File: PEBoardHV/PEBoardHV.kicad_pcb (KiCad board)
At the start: 2 copper layers, 40 parts, among them J1 To PE LV, J2 Left Connector (Master), J3 E-Meter Internal, J4 Right Connector (Slave), J5 E-Meter External, J6 HV Cable, J7 TSMPs, J8 HV CAN Debug, J9 EMeter HV, U1 L78S05CV-DG, U2 ISO1050, U3 PS2501-4, U4 DK1A1B-12V, U5 DK1A1B-12V

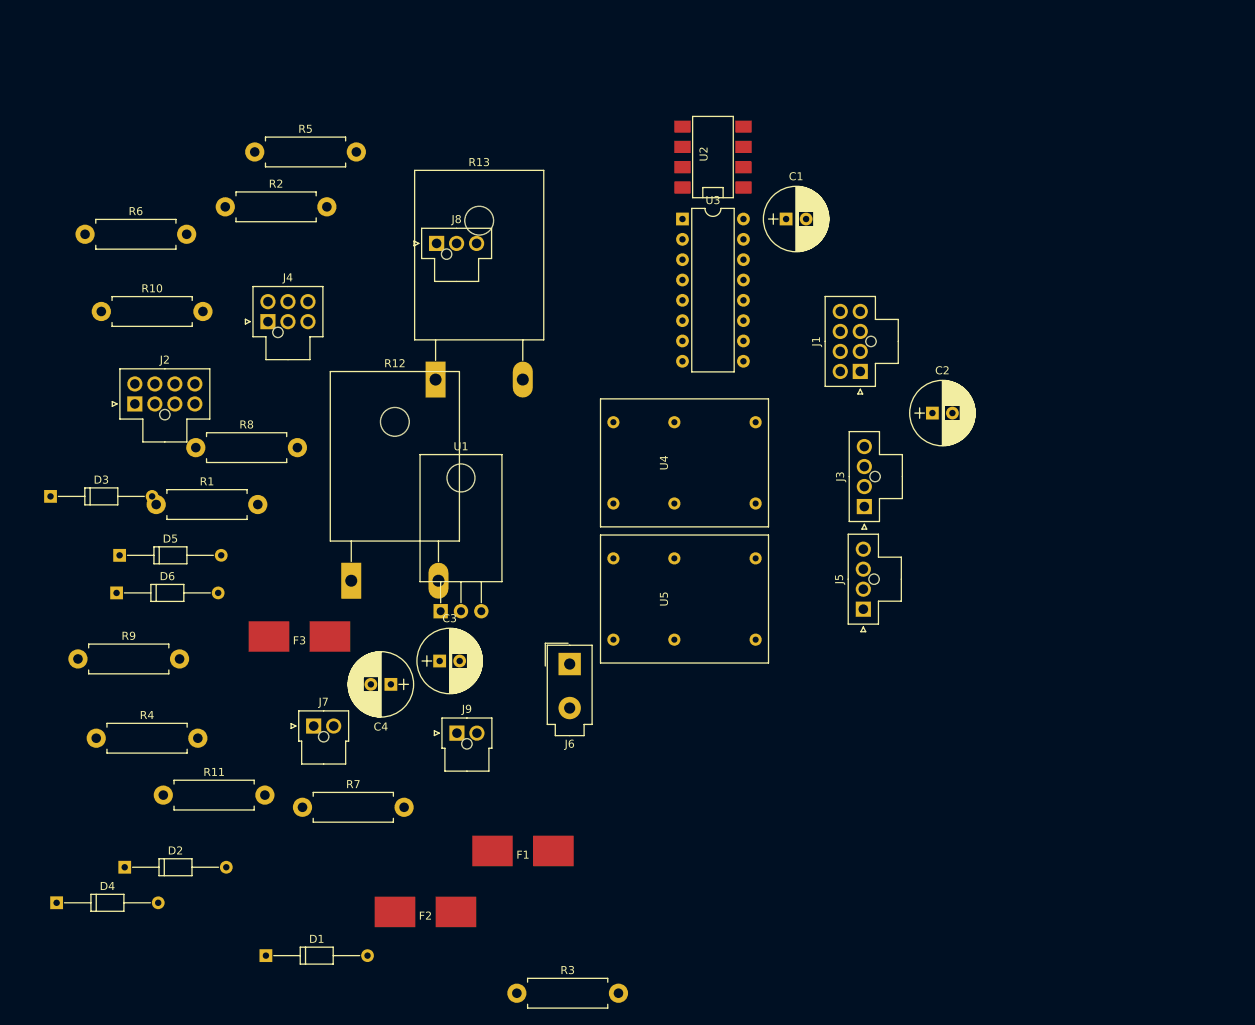
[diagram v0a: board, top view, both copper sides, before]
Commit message: Progress on PE HV PCB layout
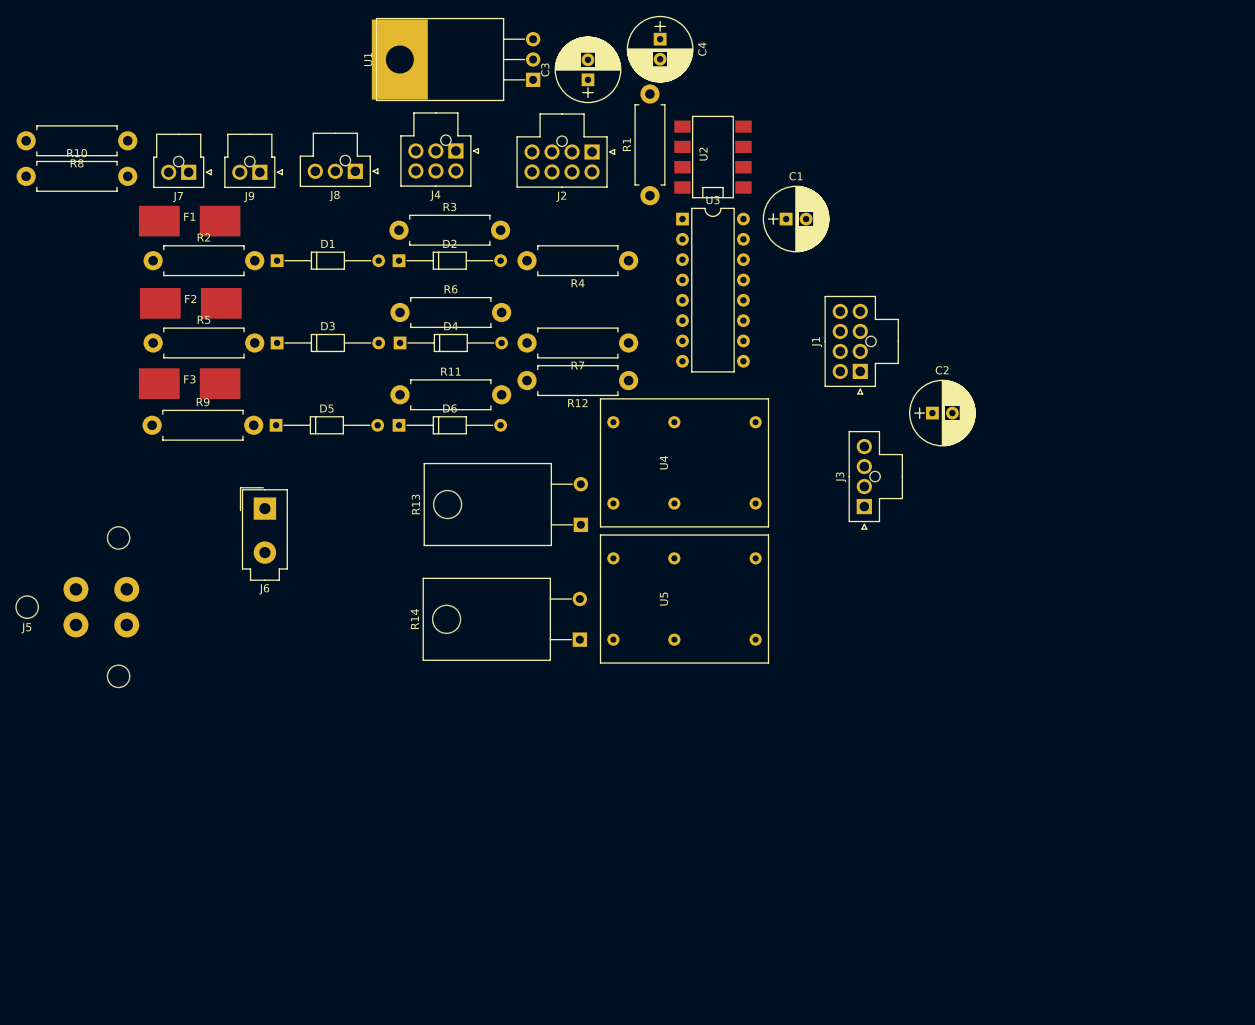
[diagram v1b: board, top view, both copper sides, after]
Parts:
- added R14: 1K, TO_SOT_Packages_THT:TO-220-2_Horizontal, F.Cu at (145.9, 112.8)
- J5: footprint Connectors_Molex:Molex_NanoFit_1x04x2.50mm_Straight -> FSFootprints:DT13-4P
- R1: value R -> 120
- R10: value 1.2kR -> 5kR
- R11, R3, R6: value 3kR -> 1.2kR
- R12: value 1K -> 3kR; footprint TO_SOT_Packages_THT:TO-247-2_Horizontal -> Resistors_THT:R_Axial_DIN0411_L9.9mm_D3.6mm_P12.70mm_Horizontal
- R13: footprint TO_SOT_Packages_THT:TO-247-2_Horizontal -> TO_SOT_Packages_THT:TO-220-2_Horizontal
- R2, R5: value 1.2kR -> R
- R4: value R -> 3kR
- R7: value 5kR -> 3kR
- R8: value R -> 5kR
- R9: value 5kR -> R
- U1: footprint TO_SOT_Packages_THT:TO-220-3_Horizontal -> FSFootprints:TO-220-3_Horizontal_HeatSunk
- moved J5 104.5 mm to (76.8, 108.7), turned to 0 degrees
- moved R3 96.5 mm to (123.3, 61.6)
- moved R4 89.4 mm to (152.0, 65.4), turned to 180 degrees
- moved F1 89.1 mm to (97.2, 60.5), turned to 180 degrees
- moved C4 87.4 mm to (156.0, 37.7), turned to 270 degrees
- moved D1 86.9 mm to (108.1, 65.4)
- moved D2 83.2 mm to (123.3, 65.4)
- moved D4 82.1 mm to (123.4, 75.7)
- moved F2 81.5 mm to (97.3, 70.7), turned to 180 degrees
- moved C3 75.0 mm to (146.9, 42.8), turned to 90 degrees
- moved J9 74.3 mm to (105.9, 54.4), turned to 180 degrees
- moved R1 72.8 mm to (154.7, 57.3), turned to 90 degrees
- moved J7 71.0 mm to (97.0, 54.4), turned to 180 degrees
- moved R7 70.9 mm to (152.0, 75.7), turned to 180 degrees
- moved U1 67.4 mm to (140.1, 42.8), turned to 90 degrees
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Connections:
- J2 pad 8: Net-(J2-Pad8) -> (no net)
- R1 pad 1: Net-(F1-Pad2) -> /CAN_H_BOARD
- R1 pad 2: Net-(D1-Pad1) -> /CAN_L_BOARD
- R10 pad 1: Net-(D5-Pad2) -> /TS-
- R10 pad 2: Net-(R10-Pad2) -> Net-(J7-Pad2)
- R11 pad 1: /TS- -> Net-(D5-Pad2)
- R11 pad 2: Net-(D6-Pad2) -> Net-(R11-Pad2)
- R12 pad 1: /TS+_SWITCHED_L -> /TS-
- R12 pad 2: Net-(R12-Pad2) -> Net-(D6-Pad2)
- R13 pad 1: /TS+_SWITCHED_R -> /TS-
- R2 pad 1: Net-(D1-Pad2) -> Net-(F1-Pad2)
- R2 pad 2: Net-(R2-Pad2) -> Net-(D1-Pad1)
- R3 pad 1: /TS- -> Net-(D1-Pad2)
- R3 pad 2: Net-(D2-Pad2) -> Net-(R3-Pad2)
- R4 pad 1: Net-(F2-Pad2) -> /TS-
- R4 pad 2: Net-(D3-Pad1) -> Net-(D2-Pad2)
- R5 pad 1: Net-(D3-Pad2) -> Net-(F2-Pad2)
- R5 pad 2: Net-(R5-Pad2) -> Net-(D3-Pad1)
- R6 pad 1: /TS- -> Net-(D3-Pad2)
- R6 pad 2: Net-(D4-Pad2) -> Net-(R6-Pad2)
- R7 pad 1: Net-(J7-Pad1) -> /TS-
- R7 pad 2: /TS+_FUSED -> Net-(D4-Pad2)
- R8 pad 1: /TS+_FUSED -> Net-(J7-Pad1)
- R8 pad 2: Net-(D5-Pad1) -> /TS+_FUSED
- R9 pad 1: /TS- -> /TS+_FUSED
- R9 pad 2: Net-(J7-Pad2) -> Net-(D5-Pad1)
- U2 pad 1: /3.3V_LV -> (no net)
- U3 pad 1: Net-(R2-Pad2) -> Net-(R3-Pad2)
- U3 pad 3: Net-(R5-Pad2) -> Net-(R6-Pad2)
- U3 pad 5: Net-(R10-Pad2) -> Net-(R11-Pad2)
- U4 pad 3: Net-(U4-Pad3) -> (no net)
- U4 pad 4: Net-(U4-Pad4) -> (no net)
- U4 pad 5: Net-(R12-Pad2) -> /TS+_SWITCHED_L
- U4 pad 6: /TS- -> Net-(R13-Pad2)
- U5 pad 3: Net-(U5-Pad3) -> (no net)
- U5 pad 4: Net-(U5-Pad4) -> (no net)
- U5 pad 5: Net-(R13-Pad2) -> /TS+_SWITCHED_R
- U5 pad 6: /TS- -> Net-(R14-Pad2)

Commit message: Layout and route PE HV board
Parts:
- added C5: CP, Capacitors_THT:CP_Radial_D8.0mm_P2.50mm, F.Cu at (110.7, 89.7)
- C1: value C -> CP
- C3: value CP -> C
- J6: footprint Connectors_Molex:Molex_MiniFit-JR-5556-02A_2x01x4.20mm_Straight -> Connectors_Molex:Molex_NanoFit_1x02x2.50mm_Straight
- J7: footprint Connectors_Molex:Molex_NanoFit_1x02x2.50mm_Straight -> FSFootprints:DT15-2P; moved to B.Cu
- R13, R14: footprint TO_SOT_Packages_THT:TO-220-2_Horizontal -> TO_SOT_Packages_THT:TO-220-2_Vertical
- moved R10 73.2 mm to (120.9, 113.2)
- moved C4 67.6 mm to (124.2, 97.4)
- moved U1 58.2 mm to (115.4, 95.5), turned to 180 degrees
- moved J7 45.2 mm to (125.9, 89.2), turned to 0 degrees
- moved J6 42.5 mm to (98.6, 54.6), turned to 180 degrees
- moved R8 35.9 mm to (119.3, 70.4)
- moved C3 29.8 mm to (173.5, 56.4)
- moved R9 27.8 mm to (88.1, 58.5), turned to 270 degrees
- moved R5 26.0 mm to (118.2, 79.6), turned to 180 degrees
- moved C1 24.2 mm to (147.7, 57.5), turned to 90 degrees
- moved F3 21.8 mm to (82.4, 64.8), turned to 90 degrees
- moved C2 16.3 mm to (175.3, 77.6), turned to 180 degrees
- moved R14 11.7 mm to (144.8, 101.1), turned to 180 degrees
- moved J1 10.9 mm to (175.0, 70.1)
- moved J3 7.69 mm to (174.4, 93.2)
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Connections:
- C1 pad 1: /5V_GLV -> /5V_TS
- C1 pad 2: GND -> /TS-
- C2 pad 1: /3.3V_GLV -> /5V_GLV
- C3 pad 1: /CAN+ -> /3.3V_GLV
- C3 pad 2: /TS- -> GND
- C4 pad 1: /5V_TS -> /CAN+
- U2 pad 1: (no net) -> /3.3V_GLV
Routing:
- net GND: track 0.00 -> 186.6 mm
- net /TS-: track 0.00 -> 181.7 mm, vias 0 -> 1
- net +12V: track 0.00 -> 146.4 mm
- net /EM_SIG-: track 0.00 -> 126.3 mm
- net /EM_SIG+: track 0.00 -> 122.2 mm
- net /TS+_SWITCHED_R: track 0.00 -> 97.8 mm
- net /TS+_SWITCHED_L: track 0.00 -> 92.5 mm
- net /5V_TS: track 0.00 -> 84.4 mm
- net /TS+: track 0.00 -> 71.2 mm, vias 0 -> 1
- net /CAN+: track 0.00 -> 64.5 mm
- net /AIRS_FINAL: track 0.00 -> 50.8 mm
- net /TS+_FUSED: track 0.00 -> 49.1 mm
- net /CAN_H_BOARD: track 0.00 -> 44.9 mm, vias 0 -> 1
- net /5V_GLV: track 0.00 -> 32.7 mm
- net Net-(J7-Pad1): track 0.00 -> 31.0 mm
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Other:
- board outline added: 104.5 x 76.3 mm

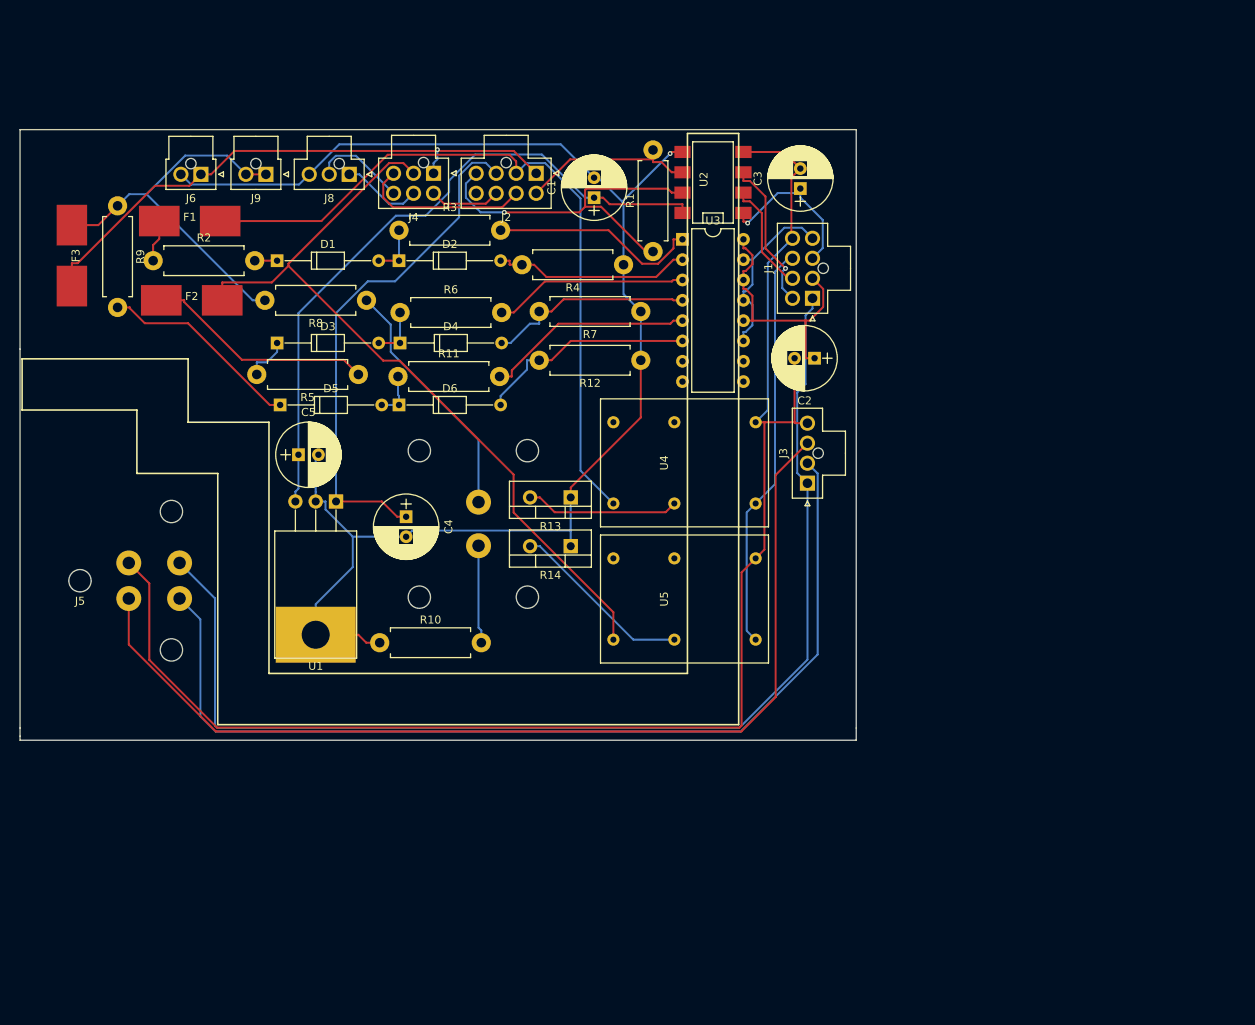
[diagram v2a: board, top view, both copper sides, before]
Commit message: Reverse direction of PE HV pcb
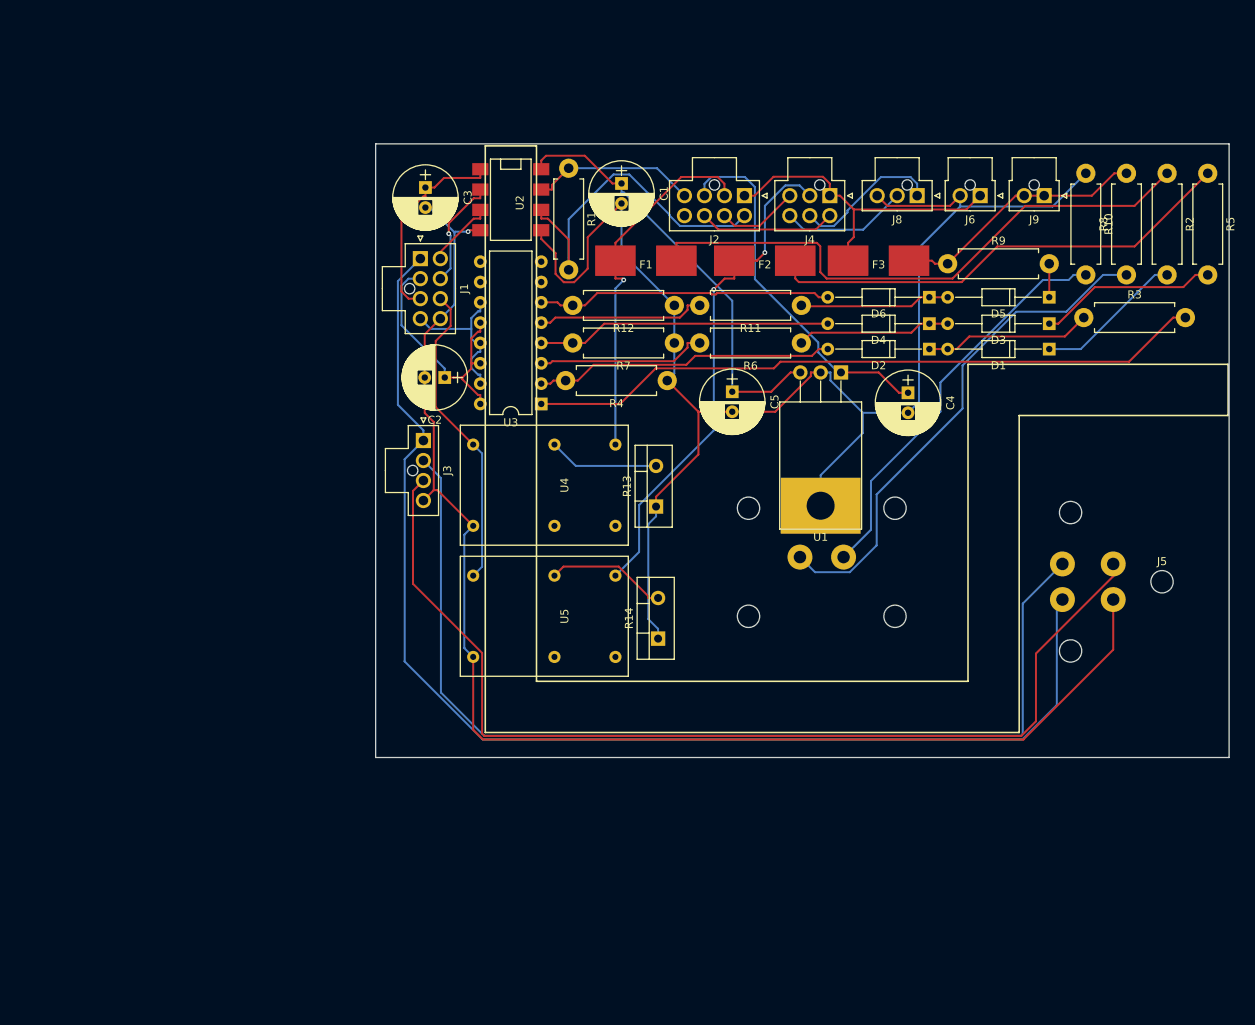
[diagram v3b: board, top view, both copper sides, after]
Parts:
- moved J5 135.3 mm to (218.7, 105.5), turned to 180 degrees
- moved R2 127.2 mm to (219.3, 54.5), turned to 270 degrees
- moved R5 109.1 mm to (224.4, 54.5), turned to 270 degrees
- moved R10 106.0 mm to (209.2, 54.5), turned to 270 degrees
- moved R9 104.0 mm to (191.9, 65.8), turned to 0 degrees
- moved F3 100.8 mm to (183.3, 65.4), turned to 0 degrees
- moved J6 97.4 mm to (196.0, 57.3)
- moved J9 97.3 mm to (204.0, 57.3)
- moved D1 97.2 mm to (204.6, 76.5), turned to 180 degrees
- moved D5 97.1 mm to (204.6, 70.0), turned to 180 degrees
- moved D3 96.6 mm to (204.6, 73.3), turned to 180 degrees
- moved R8 95.0 mm to (214.2, 67.2), turned to 90 degrees
- moved R3 86.3 mm to (208.9, 72.5)
- moved F2 71.8 mm to (169.0, 65.4), turned to 0 degrees
- moved J8 71.0 mm to (188.1, 57.3)
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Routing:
- net Net-(F1-Pad2): track 5.27 -> 72.8 mm
- net Net-(R3-Pad2): track 26.4 -> 85.0 mm
- net /TS+_SWITCHED_L: track 92.5 -> 45.5 mm, vias 0 -> 1
- net Net-(J7-Pad2): track 12.3 -> 50.6 mm
- net /TS+_SWITCHED_R: track 97.8 -> 63.6 mm, vias 0 -> 2
- net Net-(J7-Pad1): track 31.0 -> 63.9 mm
- net Net-(F2-Pad2): track 28.6 -> 59.6 mm
- net /TS+: track 71.2 -> 40.4 mm, vias 1 -> 0
- net /5V_TS: track 84.4 -> 54.3 mm
- net /CAN_H_BOARD: track 44.9 -> 20.8 mm, vias 1 -> 0
- net Net-(D5-Pad1): track 25.4 -> 4.19 mm
- net /CAN_L_BOARD: track 22.1 -> 43.3 mm
- net /CAN+: track 64.5 -> 45.9 mm
- net GND: track 186.6 -> 168.9 mm, vias 0 -> 1
- net /TS+_FUSED: track 49.1 -> 32.0 mm
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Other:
- board size 104.5 x 76.3 mm -> 106.7 x 76.7 mm

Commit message: Tweak PE HV board
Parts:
- added H1: MtngHole, Mounting_Holes:MountingHole_4.5mm, F.Cu at (125.5, 55.9)
- added H2: MtngHole, Mounting_Holes:MountingHole_4.5mm, F.Cu at (125.5, 122.4)
- C1, C2, C3, C4, C5: footprint Capacitors_THT:CP_Radial_D8.0mm_P2.50mm -> Capacitors_THT:CP_Radial_D5.0mm_P2.50mm
- J3: footprint Connectors_Molex:Molex_NanoFit_1x04x2.50mm_Straight -> Connectors_Molex:Molex_NanoFit_2x02x2.50mm_Straight
- moved C3 8.56 mm to (125.7, 64.8), turned to 0 degrees
- moved J1 5.97 mm to (125.7, 71.1)
- moved C2 5.14 mm to (128.3, 85.1)
- moved J3 3.61 mm to (125.7, 91.4)
- moved C4 1.65 mm to (185.4, 81.3)
- moved C5 1.49 mm to (166.4, 81.3)
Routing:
- net /TS-: track 187.2 -> 169.9 mm
- net /TS+: track 40.4 -> 50.7 mm
- net /TS+_SWITCHED_L: track 45.5 -> 54.0 mm
- net /CAN_L_BOARD: track 43.3 -> 35.5 mm, vias 0 -> 1
- net /AIRS_FINAL: track 38.8 -> 31.4 mm
- net /CAN_TX: track 8.64 -> 16.0 mm
- net /5V_GLV: track 32.1 -> 37.9 mm
- net /CAN_RX: track 13.9 -> 19.4 mm
- net +12V: track 154.6 -> 149.6 mm
- net GND: track 168.9 -> 163.9 mm, vias 1 -> 0
- net Net-(F1-Pad2): track 72.8 -> 69.4 mm
- net /EM_SIG+: track 128.3 -> 125.0 mm
- net /3.3V_GLV: track 25.6 -> 28.6 mm
- net /5V_TS: track 54.3 -> 52.1 mm
- net Net-(R13-Pad2): track 13.8 -> 14.9 mm
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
